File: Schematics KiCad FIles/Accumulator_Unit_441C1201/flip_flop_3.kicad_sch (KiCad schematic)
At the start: 15 parts, among them U1203 5963

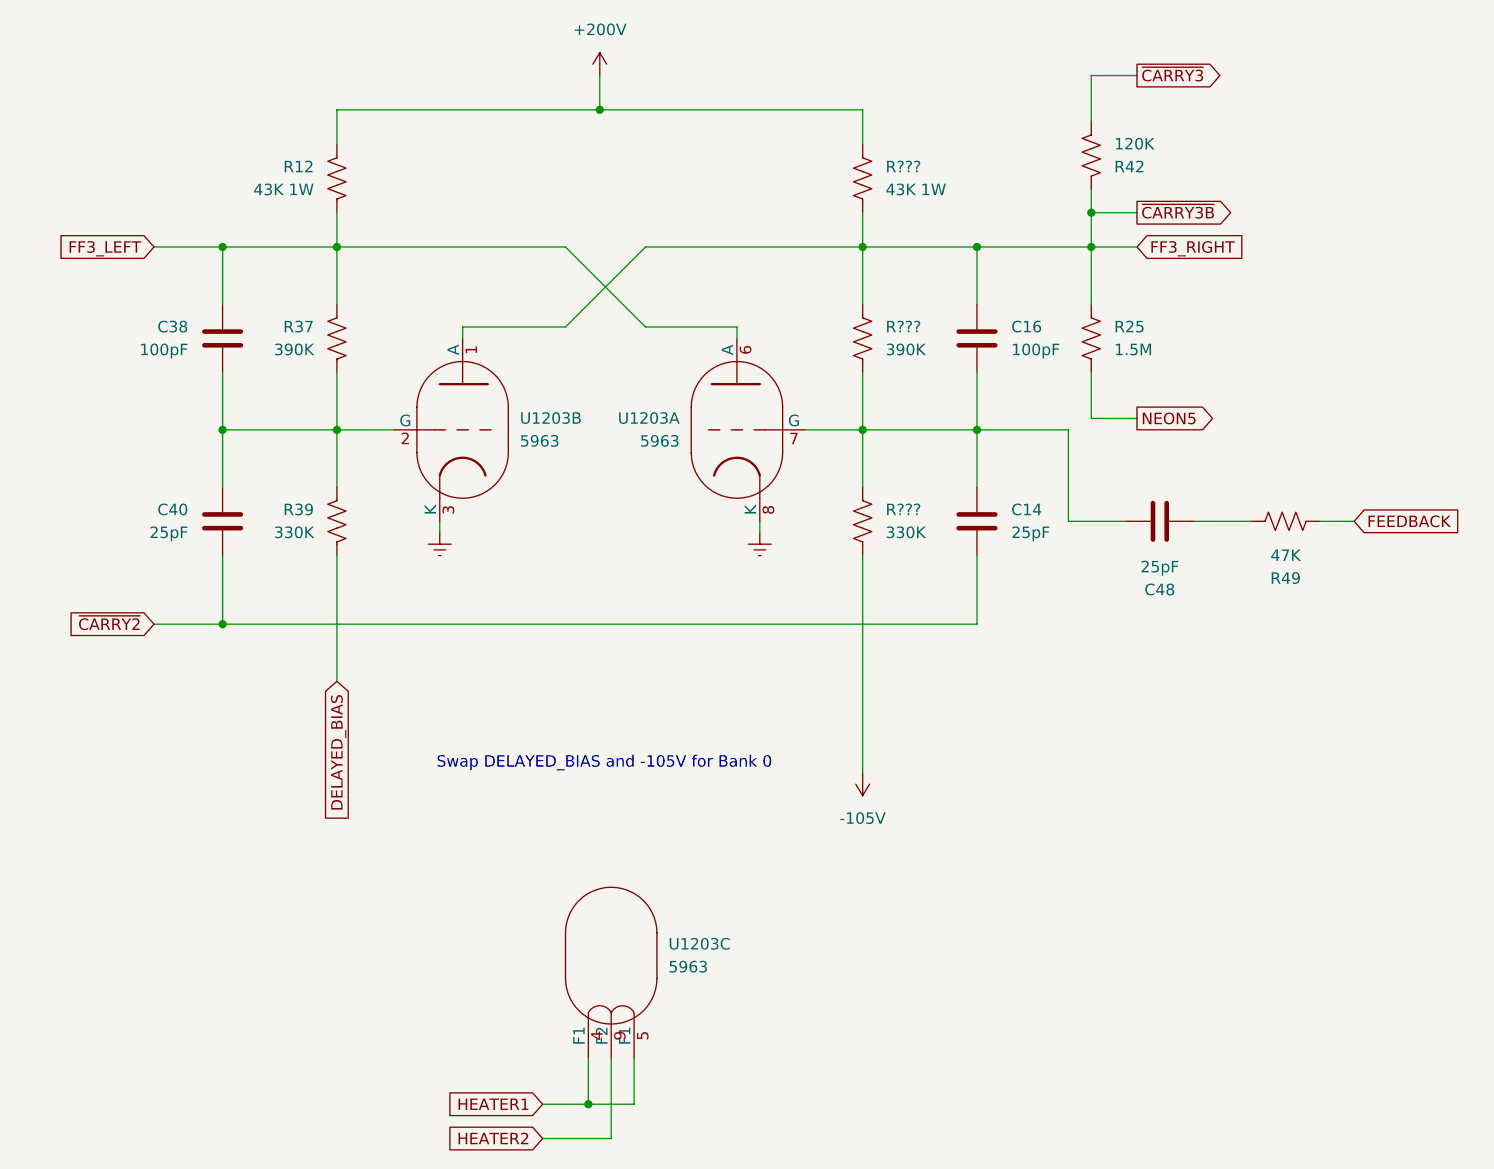
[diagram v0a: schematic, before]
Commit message: Fix component designators on accumulator schematics
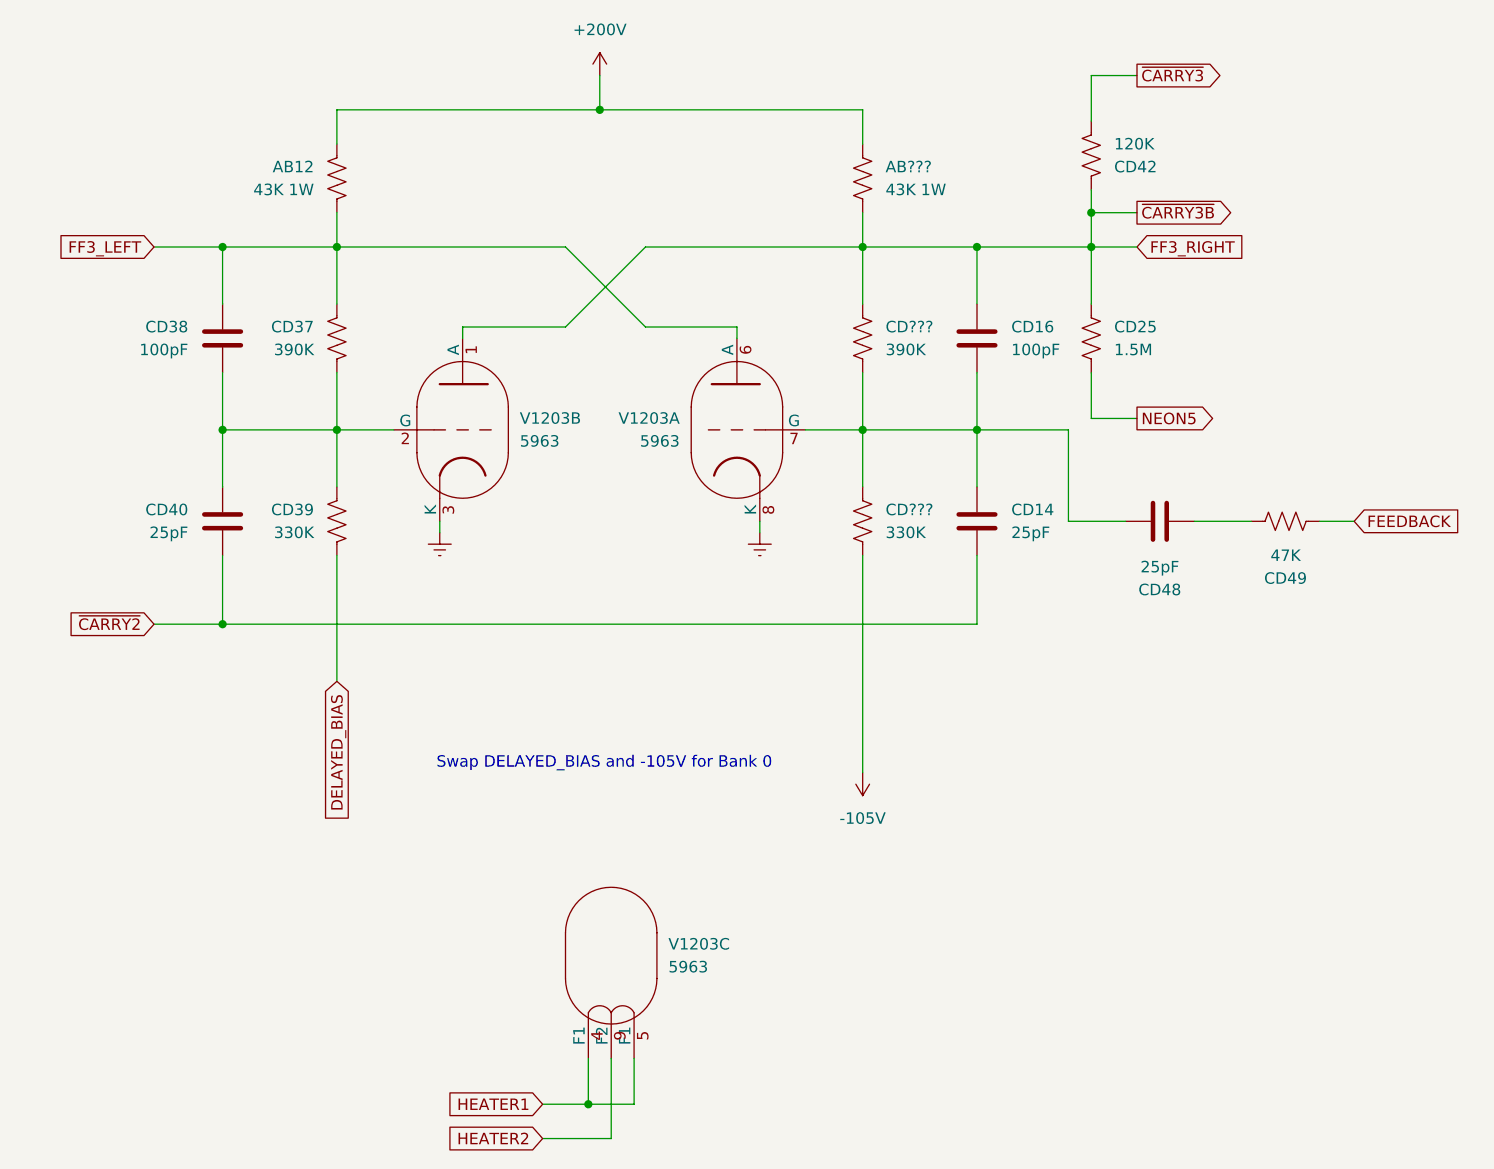
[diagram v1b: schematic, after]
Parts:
- gave numbers to parts that had none: 2
- renumbered R12 to AB12, C14 to CD14, C16 to CD16, R25 to CD25, R37 to CD37, C38 to CD38, R39 to CD39, C40 to CD40, R42 to CD42, C48 to CD48, R49 to CD49, U1203 to V1203
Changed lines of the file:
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@@
 		(on_board yes)
 		(dnp no)
-		(property "Reference" "C48"
+		(property "Reference" "CD48"
 			(at 208.28 100.33 90)
 			(effects
@@
 			(project "Accumulator_Unit_441C1201"
 				(path "/519d7692-6bf3-45ab-bd58-713783b63e8a/c9d7697e-0573-4ddc-8965-46766e8b7d72"
-					(reference "C48")
+					(reference "CD48")
 					(unit 1)
 				)
@@
 		(on_board yes)
 		(dnp no)
-		(property "Reference" "C40"
+		(property "Reference" "CD40"
 			(at 100.33 91.4399 0)
 			(effects
@@
 			(project "Accumulator_Unit_441C1201"
 				(path "/519d7692-6bf3-45ab-bd58-713783b63e8a/c9d7697e-0573-4ddc-8965-46766e8b7d72"
-					(reference "C40")
+					(reference "CD40")
 					(unit 1)
 				)
@@
 		(dnp no)
 		(fields_autoplaced yes)
-		(property "Reference" "U1203"
+		(property "Reference" "V1203"
 			(at 137.16 81.2799 0)
 			(effects
@@
 			(project "Accumulator_Unit_441C1201"
 				(path "/519d7692-6bf3-45ab-bd58-713783b63e8a/c9d7697e-0573-4ddc-8965-46766e8b7d72"
-					(reference "U1203")
+					(reference "V1203")
 					(unit 2)
 				)
@@
 		(on_board yes)
 		(dnp no)
-		(property "Reference" "R37"
+		(property "Reference" "CD37"
 			(at 114.3 71.1199 0)
 			(effects
@@
 			(project "Accumulator_Unit_441C1201"
 				(path "/519d7692-6bf3-45ab-bd58-713783b63e8a/c9d7697e-0573-4ddc-8965-46766e8b7d72"
-					(reference "R37")
+					(reference "CD37")
 					(unit 1)
 				)
@@
 		(on_board yes)
 		(dnp no)
-		(property "Reference" "C16"
+		(property "Reference" "CD16"
 			(at 191.77 71.1199 0)
 			(effects
@@
 			(project "Accumulator_Unit_441C1201"
 				(path "/519d7692-6bf3-45ab-bd58-713783b63e8a/c9d7697e-0573-4ddc-8965-46766e8b7d72"
-					(reference "C16")
+					(reference "CD16")
 					(unit 1)
 				)
@@
 		(on_board yes)
 		(dnp no)
-		(property "Reference" "R39"
+		(property "Reference" "CD39"
 			(at 114.3 91.4399 0)
 			(effects
@@
 			(project "Accumulator_Unit_441C1201"
 				(path "/519d7692-6bf3-45ab-bd58-713783b63e8a/c9d7697e-0573-4ddc-8965-46766e8b7d72"
-					(reference "R39")
+					(reference "CD39")
 					(unit 1)
 				)
@@
 		(on_board yes)
 		(dnp no)
-		(property "Reference" "R25"
+		(property "Reference" "CD25"
 			(at 203.2 71.1199 0)
 			(effects
@@
 			(project "Accumulator_Unit_441C1201"
 				(path "/519d7692-6bf3-45ab-bd58-713783b63e8a/c9d7697e-0573-4ddc-8965-46766e8b7d72"
-					(reference "R25")
+					(reference "CD25")
 					(unit 1)
 				)
@@
 		(on_board yes)
 		(dnp no)
-		(property "Reference" "R???"
+		(property "Reference" "CD???"
 			(at 177.8 71.1199 0)
 			(effects
@@
 			(project "Accumulator_Unit_441C1201"
 				(path "/519d7692-6bf3-45ab-bd58-713783b63e8a/c9d7697e-0573-4ddc-8965-46766e8b7d72"
-					(reference "R???")
+					(reference "CD???")
 					(unit 1)
 				)
@@
 		(on_board yes)
 		(dnp no)
-		(property "Reference" "R???"
+		(property "Reference" "AB???"
 			(at 177.8 53.3399 0)
 			(effects
@@
 			(project "Accumulator_Unit_441C1201"
 				(path "/519d7692-6bf3-45ab-bd58-713783b63e8a/c9d7697e-0573-4ddc-8965-46766e8b7d72"
-					(reference "R???")
+					(reference "AB???")
 					(unit 1)
 				)
@@
 		(on_board yes)
 		(dnp no)
-		(property "Reference" "R???"
+		(property "Reference" "CD???"
 			(at 177.8 91.4399 0)
 			(effects
@@
 			(project "Accumulator_Unit_441C1201"
 				(path "/519d7692-6bf3-45ab-bd58-713783b63e8a/c9d7697e-0573-4ddc-8965-46766e8b7d72"
-					(reference "R???")
+					(reference "CD???")
 					(unit 1)
 				)
@@
 		(on_board yes)
 		(dnp no)
-		(property "Reference" "C14"
+		(property "Reference" "CD14"
 			(at 191.77 91.4399 0)
 			(effects
@@
 			(project "Accumulator_Unit_441C1201"
 				(path "/519d7692-6bf3-45ab-bd58-713783b63e8a/c9d7697e-0573-4ddc-8965-46766e8b7d72"
-					(reference "C14")
+					(reference "CD14")
 					(unit 1)
 				)
@@
 		(on_board yes)
 		(dnp no)
-		(property "Reference" "C38"
+		(property "Reference" "CD38"
 			(at 100.33 71.1199 0)
 			(effects
@@
 			(project "Accumulator_Unit_441C1201"
 				(path "/519d7692-6bf3-45ab-bd58-713783b63e8a/c9d7697e-0573-4ddc-8965-46766e8b7d72"
-					(reference "C38")
+					(reference "CD38")
 					(unit 1)
 				)
@@
 		(on_board yes)
 		(dnp no)
-		(property "Reference" "R12"
+		(property "Reference" "AB12"
 			(at 114.3 53.3399 0)
 			(effects
@@
 			(project "Accumulator_Unit_441C1201"
 				(path "/519d7692-6bf3-45ab-bd58-713783b63e8a/c9d7697e-0573-4ddc-8965-46766e8b7d72"
-					(reference "R12")
+					(reference "AB12")
 					(unit 1)
 				)
@@
 		(on_board yes)
 		(dnp no)
-		(property "Reference" "U1203"
+		(property "Reference" "V1203"
 			(at 154.94 81.2799 0)
 			(effects
@@
 			(project "Accumulator_Unit_441C1201"
 				(path "/519d7692-6bf3-45ab-bd58-713783b63e8a/c9d7697e-0573-4ddc-8965-46766e8b7d72"
-					(reference "U1203")
+					(reference "V1203")
 					(unit 1)
 				)
@@
 		(on_board yes)
 		(dnp no)
-		(property "Reference" "R42"
+		(property "Reference" "CD42"
 			(at 203.2 53.3401 0)
 			(effects
@@
 			(project "Accumulator_Unit_441C1201"
 				(path "/519d7692-6bf3-45ab-bd58-713783b63e8a/c9d7697e-0573-4ddc-8965-46766e8b7d72"
-					(reference "R42")
+					(reference "CD42")
 					(unit 1)
 				)
@@
 		(dnp no)
 		(fields_autoplaced yes)
-		(property "Reference" "U1203"
+		(property "Reference" "V1203"
 			(at 153.67 139.6999 0)
 			(effects
@@
 			(project "Accumulator_Unit_441C1201"
 				(path "/519d7692-6bf3-45ab-bd58-713783b63e8a/c9d7697e-0573-4ddc-8965-46766e8b7d72"
-					(reference "U1203")
+					(reference "V1203")
 					(unit 3)
 				)
@@
 		(on_board yes)
 		(dnp no)
-		(property "Reference" "R49"
+		(property "Reference" "CD49"
 			(at 222.25 99.06 90)
 			(effects
@@
 			(project "Accumulator_Unit_441C1201"
 				(path "/519d7692-6bf3-45ab-bd58-713783b63e8a/c9d7697e-0573-4ddc-8965-46766e8b7d72"
-					(reference "R49")
-					(unit 1)
-				)
+					(reference "CD49")
+					(unit 1)
+				)
